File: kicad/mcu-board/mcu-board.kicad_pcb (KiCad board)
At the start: 2 copper layers, 53 parts, among them J1 Conn_01x03, J10 Conn_01x03, J11 Conn_01x02, J12 Conn_01x02, J13 UJ20-C-H-G-SMT-P16-TR, J2 Conn_01x09_Pin, J3 Conn_01x03, J4 Conn_01x10, J6 Conn_01x03, J7 Conn_01x03, J8 Conn_01x04, J9 Conn_01x02, Q1 Q_NPN_CEB, SW1 SW_Push, U1 AP3445LW6-7, U2 Lora1276-C1-868, U3 ESP32-S3-WROOM-1U-N16R8, U4 LM66200DRLR

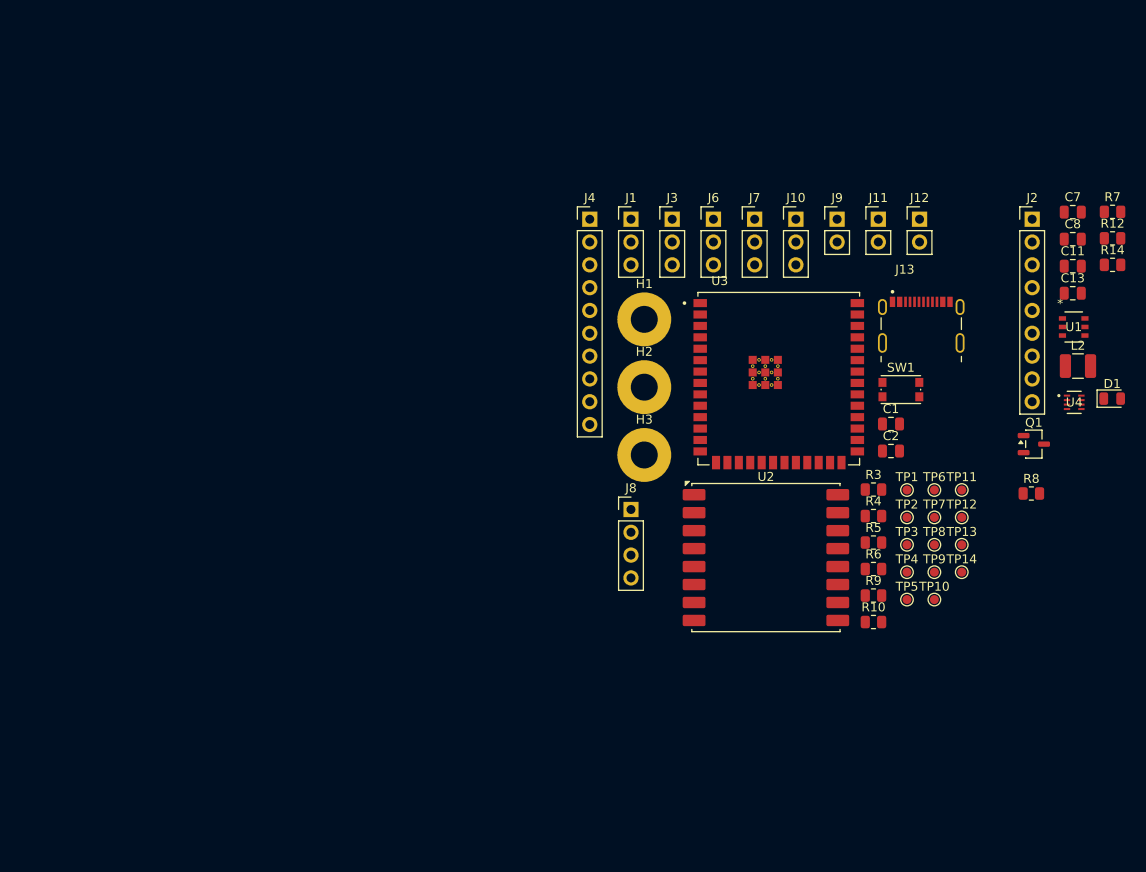
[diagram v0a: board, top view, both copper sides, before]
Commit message: chore?: Saving just in case I screw up something when redoing the board with battery cutout.
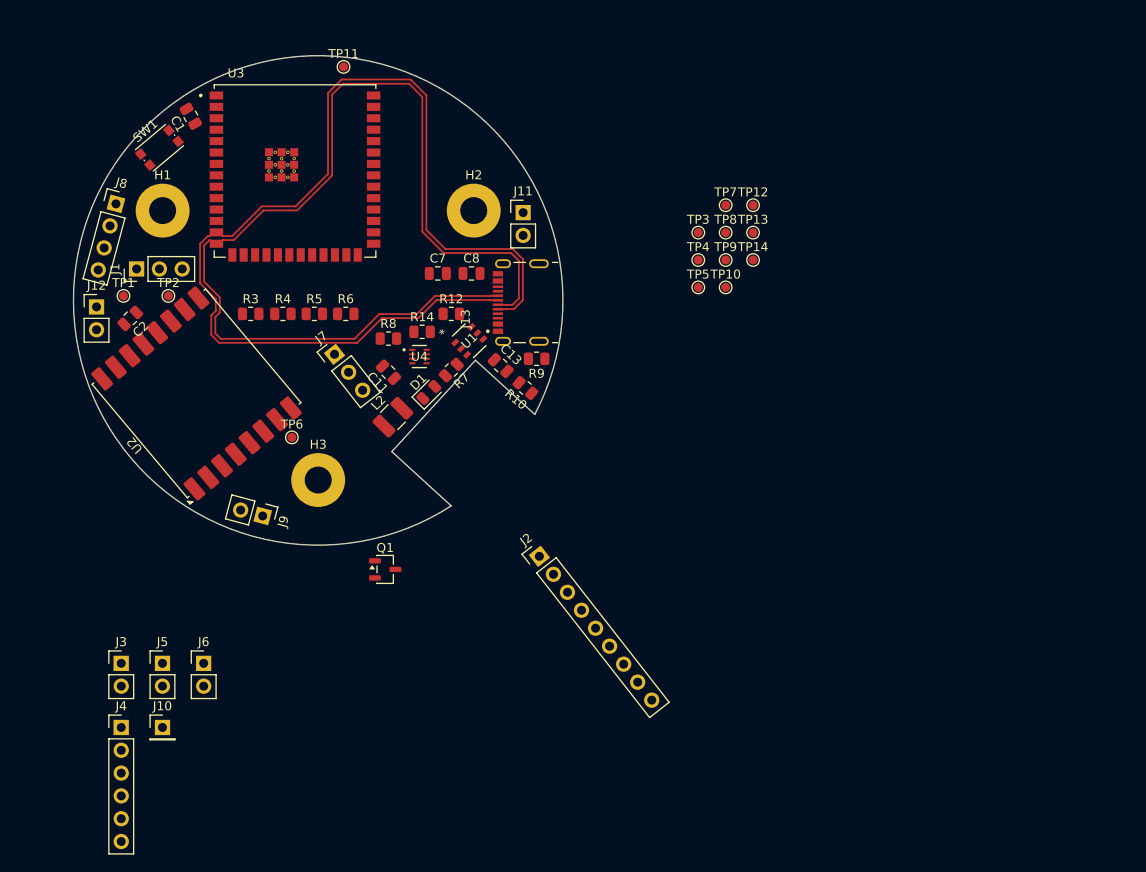
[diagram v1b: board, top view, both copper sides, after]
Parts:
- added J5: Conn_01x02, Connector_PinHeader_2.54mm:PinHeader_1x02_P2.54mm_Vertical, F.Cu at (87.3, 138.9)
- J10: value Conn_01x03 -> Conn_01x01; footprint Connector_PinHeader_2.54mm:PinHeader_1x03_P2.54mm_Vertical -> Connector_PinHeader_2.54mm:PinHeader_1x01_P2.54mm_Vertical
- J3, J6: value Conn_01x03 -> Conn_01x02; footprint Connector_PinHeader_2.54mm:PinHeader_1x03_P2.54mm_Vertical -> Connector_PinHeader_2.54mm:PinHeader_1x02_P2.54mm_Vertical
- J4: value Conn_01x10 -> Conn_01x06; footprint Connector_PinHeader_2.54mm:PinHeader_1x10_P2.54mm_Vertical -> Connector_PinHeader_2.54mm:PinHeader_1x06_P2.54mm_Vertical
- moved J12 92.2 mm to (80.0, 99.2)
- moved J10 90.4 mm to (87.3, 146.1)
- moved TP1 89.9 mm to (83.0, 98.0)
- moved SW1 86.8 mm to (87.0, 81.5), turned to 40 degrees
- moved C2 86.0 mm to (83.8, 100.5), turned to -136 degrees
- moved TP2 85.9 mm to (88.0, 98.0)
- moved C1 85.2 mm to (90.5, 78.0), turned to 120 degrees
- moved TP11 83.4 mm to (107.5, 72.5)
- moved J3 78.8 mm to (82.8, 138.9)
- moved R14 77.2 mm to (116.2, 102.0)
- moved C11 77.1 mm to (112.5, 106.5), turned to 134 degrees
- moved J4 77.0 mm to (82.8, 146.1)
- moved L2 76.5 mm to (113.0, 111.5), turned to 45 degrees
- moved D1 76.1 mm to (117.0, 108.8), turned to 45 degrees
- moved R7 75.7 mm to (119.5, 106.2), turned to -136 degrees
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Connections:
- net Net-(AE1-A) renamed /ANT
- J10 pad 1: /I2CEXT1_SDA -> GND
- J6 pad 1: /I2CEXT0_SDA -> /I2CEXT1_SDA
- J6 pad 2: /I2CEXT0_SCL -> /I2CEXT1_SCL
- U3 pad 16: /GPIO46 -> unconnected-(U3-IO46-Pad16)
- U3 pad 24: /GPIO47 -> unconnected-(U3-IO47-Pad24)
- U3 pad 25: /GPIO48 -> unconnected-(U3-IO48-Pad25)
- U3 pad 26: /GPIO45 -> unconnected-(U3-IO45-Pad26)
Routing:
- net /D-: track 0.00 -> 119.3 mm
- net /D+: track 0.00 -> 116.3 mm
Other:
- board outline added: 54.5 x 54.5 mm

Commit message: chore?: Saving again, might redo pcb
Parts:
- removed C11: 22pF, Capacitor_SMD:C_0805_2012Metric
- removed C13, C8: 22uF, Capacitor_SMD:C_0805_2012Metric
- removed J1: Conn_01x03, Connector_PinHeader_2.54mm:PinHeader_1x03_P2.54mm_Vertical
- removed L2: 2u2H, Inductor_SMD:L_1210_3225Metric
- removed R12: 450K, Resistor_SMD:R_0805_2012Metric
- removed R14: 100K, Resistor_SMD:R_0805_2012Metric
- added C3: 22uF, Capacitor_SMD:C_0805_2012Metric, B.Cu at (100.8, 107.0)
- added C4: 22uF, Capacitor_SMD:C_0805_2012Metric, B.Cu at (100.8, 105.0)
- added C5: 22pF, Capacitor_SMD:C_0805_2012Metric, B.Cu at (100.8, 101.0)
- added C6: 22uF, Capacitor_SMD:C_0805_2012Metric, B.Cu at (100.8, 109.0)
- added L1: 2u2H, PSAT_Library:IND_SPM6530T-1R5M100, B.Cu at (95.6, 101.0)
- added R1: 4.7k, Resistor_SMD:R_0805_2012Metric, F.Cu at (107.5, 94.7)
- added R11: 5.1k, Resistor_SMD:R_0805_2012Metric, B.Cu at (88.9, 109.3)
- added R2: 4.7k, Resistor_SMD:R_0805_2012Metric, F.Cu at (121.0, 92.0)
- added TP15: TestPoint, TestPoint:TestPoint_Pad_D1.0mm, B.Cu at (120.4, 94.7)
- added TP16: TestPoint, TestPoint:TestPoint_Pad_D1.0mm, B.Cu at (124.4, 94.8)
- C2, Q1, SW1, TP1, TP10, TP11, TP12, TP13, TP14, TP2, TP3, TP4, TP5, TP6, TP7, TP8, TP9: moved to B.Cu
- C7: value 22uF -> 0.1uf; moved to B.Cu
- H1, H2, H3: footprint MountingHole:MountingHole_3mm_Pad -> PSAT_Library:Mounting-Hole-3mm-0.05mm-pad
- J10: value Conn_01x01 -> Conn_01x02; footprint Connector_PinHeader_2.54mm:PinHeader_1x01_P2.54mm_Vertical -> Connector_PinHeader_2.54mm:PinHeader_1x02_P2.54mm_Vertical
- J12: value Conn_01x02 -> UJ20-C-H-G-SMT-P16-TR; footprint Connector_PinHeader_2.54mm:PinHeader_1x02_P2.54mm_Vertical -> PSAT_Library:SAMESKY_UJ20-C-H-G-SMT-P16-TR
- J13: value UJ20-C-H-G-SMT-P16-TR -> Conn_01x06; footprint PSAT_Library:SAMESKY_UJ20-C-H-G-SMT-P16-TR -> Connector_PinHeader_2.54mm:PinHeader_1x06_P2.54mm_Vertical
- J2: value Conn_01x09_Pin -> Conn_01x06; footprint Connector_PinHeader_2.54mm:PinHeader_1x09_P2.54mm_Vertical -> Connector_PinHeader_2.54mm:PinHeader_1x06_P2.54mm_Vertical
- J3: value Conn_01x02 -> Conn_01x01; footprint Connector_PinHeader_2.54mm:PinHeader_1x02_P2.54mm_Vertical -> Connector_PinHeader_2.54mm:PinHeader_1x01_P2.54mm_Vertical
- J4: value Conn_01x06 -> Conn_01x02; footprint Connector_PinHeader_2.54mm:PinHeader_1x06_P2.54mm_Vertical -> Connector_PinHeader_2.54mm:PinHeader_1x02_P2.54mm_Vertical
- R10: value 5.1k -> 10k; moved to B.Cu
- R5, R6: value 4.7k -> 5.1k
- R7: value 2.2K -> 450K; moved to B.Cu
- R8: value 10k -> 100K; moved to B.Cu
- R9: value 5.1k -> 2.2K
- U1: value AP3445LW6-7 -> Lora1276-C1-868; footprint PSAT_Library:SOT26_AP3445_DIO-L -> PSAT_Library:Lora1276-C1-868
- U2: value Lora1276-C1-868 -> ESP32-S3-WROOM-1U-N16R8; footprint PSAT_Library:Lora1276-C1-868 -> PSAT_Library:XCVR_ESP32-S3-WROOM-1U-N16R8
- U3: value ESP32-S3-WROOM-1U-N16R8 -> LM66200DRLR; footprint PSAT_Library:XCVR_ESP32-S3-WROOM-1U-N16R8 -> footprints:SOT-5X3_DRL_TEX
- U4: value LM66200DRLR -> AP3445LW6-7; footprint footprints:SOT-5X3_DRL_TEX -> PSAT_Library:SOT26_AP3445_DIO-L
- moved TP13 59.5 mm to (102.2, 121.8), turned to 180 degrees
- moved J5 56.3 mm to (113.8, 89.2)
- moved J6 55.9 mm to (117.5, 89.2)
- moved TP10 54.8 mm to (95.8, 90.0), turned to 180 degrees
- moved J4 52.1 mm to (103.0, 98.1), turned to 180 degrees
- moved J2 50.0 mm to (93.2, 92.4), turned to -77 degrees
- moved J8 47.2 mm to (115.9, 120.8), turned to -132.4 degrees
- moved C1 45.9 mm to (130.2, 101.0), turned to 90 degrees
- moved J9 39.8 mm to (82.8, 86.0), turned to -20 degrees
- moved TP3 39.6 mm to (107.5, 88.5), turned to 180 degrees
- moved R10 39.5 mm to (89.0, 100.6), turned to 180 degrees
- moved TP12 38.8 mm to (118.8, 106.0), turned to 180 degrees
- moved TP11 38.7 mm to (120.0, 109.2), turned to 180 degrees
- moved TP9 37.6 mm to (114.8, 107.3), turned to 180 degrees
- moved C7 33.2 mm to (88.9, 111.5)
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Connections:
- C7 pad 1: GND -> /ESP_RESET
- C7 pad 2: +3V3_USB -> GND
- J10 pad 1: GND -> +5V_FUSED
- J2 pad 1: V_USB -> GND
- J2 pad 2: /V_BAT/2 -> /ADC1_CH2
- J2 pad 3: unconnected-(J2-Pin_3-Pad3) -> /GPIO39
- J2 pad 4: unconnected-(J2-Pin_4-Pad4) -> /GPIO40
- J2 pad 5: GND -> /GPIO41
- J2 pad 6: +5V_FUSED -> /GPIO42
- J3 pad 1: /U1RX -> GND
- J4 pad 1: GND -> /U1RX
- J4 pad 2: /ADC1_CH2 -> /U1TX
- R10 pad 1: GND -> /BUZZER
- R10 pad 2: Net-(J13-CC2) -> Net-(Q1-B)
- R3 pad 1: /I2CEXT0_SDA -> +3V3
- R3 pad 2: Net-(R3-Pad2) -> /I2CEXT0_SCL
- R4 pad 1: Net-(R3-Pad2) -> +3V3
- R4 pad 2: /I2CEXT0_SCL -> /I2CEXT1_SCL
- R5 pad 1: /I2CEXT0_SDA -> GND
- R5 pad 2: Net-(R5-Pad2) -> Net-(J12-CC1)
- R6 pad 1: Net-(R5-Pad2) -> GND
- R6 pad 2: /I2CEXT0_SCL -> Net-(J12-CC2)
- R7 pad 1: V_USB -> Net-(U4-FB)
- R7 pad 2: Net-(D1-A) -> +3V3_USB
- R8 pad 1: /BUZZER -> Net-(U4-FB)
- R8 pad 2: Net-(Q1-B) -> GND
- R9 pad 1: GND -> V_USB
- R9 pad 2: Net-(J13-CC1) -> Net-(D1-A)
- SW1 pad 1: +3V3 -> GND
- TP1 pad 1: /LoRa_IRQ -> GND
- TP10 pad 1: /POWER_ST -> /V_BAT/2
- TP11 pad 1: /V_BAT/2 -> /POWER_ST
- TP2 pad 1: Net-(U2-DI1) -> /I2CEXT0_SDA
- TP3 pad 1: Net-(U2-DI2) -> /I2CEXT0_SCL
- TP4 pad 1: Net-(U2-DI3) -> Net-(U1-DI1)
- TP5 pad 1: Net-(U2-DI4) -> Net-(U1-DI2)
- TP6 pad 1: Net-(U2-DI5) -> Net-(U1-DI3)
- TP7 pad 1: Net-(R5-Pad2) -> Net-(U1-DI4)
- TP8 pad 1: Net-(R3-Pad2) -> /LoRa_IRQ
- TP9 pad 1: /ADC1_CH0 -> Net-(U1-DI5)
- U1 pad 1: V_USB -> GND
- U1 pad 2: GND -> /SPI3_Q
- U1 pad 3: Net-(U1-LX) -> /SPI3_D
- U1 pad 4: V_USB -> /SPI3_CLK
- U1 pad 5: Net-(D1-K) -> /SPI3_CS0_O
- U1 pad 6: Net-(U1-FB) -> /~{LoRa_EN}
- U2 pad 10: GND -> /POWER_ST
- U2 pad 11: Net-(U2-DI3) -> unconnected-(U2-IO18-Pad11)
- U2 pad 12: Net-(U2-DI4) -> /SERVO_PWM
- U2 pad 13: +3V3 -> /D-
- U2 pad 14: /LoRa_IRQ -> /D+
- U2 pad 15: Net-(U2-DI1) -> /SPI3_CLK
- U2 pad 16: Net-(U2-DI2) -> unconnected-(U2-IO46-Pad16)
- U2 pad 2: /SPI3_Q -> +3V3
- U2 pad 3: /SPI3_D -> /ESP_RESET
- U2 pad 4: /SPI3_CLK -> /SPI3_CS0_O
- U2 pad 5: /SPI3_CS0_O -> /SPI3_CS1_O
- U2 pad 6: /~{LoRa_EN} -> /SPI3_D
- U2 pad 7: Net-(U2-DI5) -> /SPI3_Q
- U2 pad 8: GND -> /~{LoRa_EN}
- U2 pad 9: /ANT -> /LoRa_IRQ
- U3 pad 3: /ESP_RESET -> +3V3_USB
- U3 pad 4: /SPI3_CS0_O -> GND
- U3 pad 5: /SPI3_CS1_O -> GND
- U3 pad 6: /SPI3_D -> +3V3_PSU_UNFUSED
- U3 pad 7: /SPI3_Q -> +3V3
- U3 pad 8: /~{LoRa_EN} -> /POWER_ST
- U4 pad 1: GND -> V_USB
- U4 pad 2: +3V3 -> GND
- U4 pad 3: +3V3_USB -> Net-(U4-LX)
- U4 pad 4: GND -> V_USB
- U4 pad 5: GND -> Net-(D1-K)
- U4 pad 6: +3V3_PSU_UNFUSED -> Net-(U4-FB)
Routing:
- net GND: track 0.00 -> 130.8 mm, vias 0 -> 44
- net BUZ_GND: track 0.00 -> 128.1 mm, vias 0 -> 10
- net +3V3: track 0.00 -> 124.8 mm, vias 0 -> 15
- net +5V_FUSED: track 0.00 -> 117.1 mm, vias 0 -> 2
- net /D-: track 119.3 -> 6.99 mm
- net /D+: track 116.3 -> 7.60 mm
- net V_USB: track 0.00 -> 100.9 mm, vias 0 -> 7
- net /POWER_ST: track 0.00 -> 76.2 mm, vias 0 -> 6
- net Net-(U4-FB): track 0.00 -> 62.7 mm, vias 0 -> 11
- net /SPI3_D: track 0.00 -> 62.5 mm, vias 0 -> 4
- net /SPI3_Q: track 0.00 -> 58.2 mm, vias 0 -> 3
- net /LoRa_IRQ: track 0.00 -> 57.0 mm, vias 0 -> 4
- net /SPI3_CS0_O: track 0.00 -> 55.7 mm, vias 0 -> 4
- net /~{LoRa_EN}: track 0.00 -> 48.0 mm, vias 0 -> 2
- net +3V3_PSU_UNFUSED: track 0.00 -> 45.8 mm, vias 0 -> 8
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- added copper zone on B.Cu, net GND
- added copper zone on F.Cu, net GND
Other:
- board size 54.5 x 54.5 mm -> 54.5 x 46.3 mm
- board text added: "5V_F"
- board text added: "BUZ_GND"
- board text added: "I2C0_SCL"
- board text added: "I2C0_SDA"
- board text added: "I2C1_SCL"
- board text added: "I2C1_SDA"

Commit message: feat: finished the mcu-board?
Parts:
- added G***: LOGO, LOGO, F.Cu at (83.6, 109.0)
- added G***: LOGO, LOGO, F.Cu at (121.7, 101.8)
- added G***: LOGO, LOGO, F.Cu at (89.4, 100.2)
- added G***: LOGO, LOGO, F.Cu at (116.5, 106.5)
- added G***: LOGO, LOGO, F.Cu at (96.7, 107.5)
- added G***: LOGO, LOGO, F.Cu at (116.5, 98.2)
- added SW2: SW_Push, Button_Switch_SMD:SW_Push_1P1T_NO_CK_KMR2, B.Cu at (82.2, 103.8)
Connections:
- net Net-(U1-DI1) renamed /DI1
- net Net-(U1-DI2) renamed /DI2
- net Net-(U1-DI3) renamed /DI3
- net Net-(U1-DI4) renamed /DI4
- net Net-(U1-DI5) renamed /DI5
- U2 pad 27: unconnected-(U2-IO0-Pad27) -> Net-(U2-IO0)
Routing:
- net Net-(U2-IO0): track 0.00 -> 25.7 mm, vias 0 -> 1
- net GND: track 130.8 -> 122.7 mm, vias 44 -> 45
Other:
- board text added: "3V3F 3V3U 5VF GND VBAT/2 VUSB"
- board text added: "5VF"
- board text added: "Allegedly at the current distance (trace length of ~7mm), for the usb 2.0 (full speed - 12mbps) diff pair, length and impedence matching should not be a problem."
- board text added: "BGND"
- board text added: "BOOT"
- board text added: "CAM"
- board text added: "CLK CS Q D"
- board text added: "DI1 DI2"
- board text added: "DI3 DI4"
- board text added: "DI5"
- board text added: "Designed by: aids (might be cooked)"
- board text added: "EN"
- board text added: "GND"
- board text added: "GND ADC1-2 IO39 IO40 IO41 IO42"
- board text added: "IO10 IO9"
- board text added: "LoRa_IRQ"
- board text added: "MCU-BOARD REV 1"
- board text added: "POWER_ST"
- board text added: "SCL0"
- board text added: "SCL0 SCL1"
- board text added: "SCL1"
- board text added: "SDA0"
- board text added: "SDA0 SDA1"
- board text added: "SDA1"
- board text added: "SPI3"
- board text added: "THE_RETIVERS"
- board text added: "U1RX"
- board text added: "U1TX"
- board text added: "VBAT/2"
- board text added: "V_USB"
- board text added: "{dblquote}I apologise Miguel{dblquote}"
- board text removed: "I2C0_SCL"
- board text removed: "I2C0_SDA"
- board text removed: "I2C1_SCL"
- board text removed: "I2C1_SDA"
